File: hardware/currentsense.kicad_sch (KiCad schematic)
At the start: 12 parts, among them U801 CC6900SO-5A, U802 CC6900SO-5A, U803 CC6900SO-5A

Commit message: finish component selection
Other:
- company: (none) -> matei repair lab
- title: (none) -> HALL CURRENT SENSING
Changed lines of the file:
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@@
 (kicad_sch (version 20230121) (generator eeschema)
   (paper "A4")
+  (title_block
+    (title "HALL CURRENT SENSING")
+    (date "2023-10-11")
+    (rev "0.1")
+    (company "matei repair lab")
+  )
   (junction (at 113.03 88.9) (diameter 0) (color 0 0 0 0)
   )
@@
     (pin "1")
     (instances
-      (project "sfoc-stepper"
+      (project "lemon-pepper"
         (path "/0306e2fa-4433-4288-91d9-65a3484207ad/41d11f3b-333a-47c0-a126-1f991ee11e83"
           (reference "#PWR0803") (unit 1)
@@
     (pin "2")
     (instances
-      (project "sfoc-stepper"
+      (project "lemon-pepper"
         (path "/0306e2fa-4433-4288-91d9-65a3484207ad/41d11f3b-333a-47c0-a126-1f991ee11e83"
           (reference "R806") (unit 1)
@@
     (pin "1")
     (instances
-      (project "sfoc-stepper"
+      (project "lemon-pepper"
         (path "/0306e2fa-4433-4288-91d9-65a3484207ad/41d11f3b-333a-47c0-a126-1f991ee11e83"
           (reference "#PWR0804") (unit 1)
@@
     (pin "1")
     (instances
-      (project "sfoc-stepper"
+      (project "lemon-pepper"
         (path "/0306e2fa-4433-4288-91d9-65a3484207ad/41d11f3b-333a-47c0-a126-1f991ee11e83"
           (reference "#PWR0801") (unit 1)
@@
     (pin "8")
     (instances
-      (project "sfoc-stepper"
+      (project "lemon-pepper"
         (path "/0306e2fa-4433-4288-91d9-65a3484207ad/41d11f3b-333a-47c0-a126-1f991ee11e83"
           (reference "U802") (unit 1)
@@
     (pin "1")
     (instances
-      (project "sfoc-stepper"
+      (project "lemon-pepper"
         (path "/0306e2fa-4433-4288-91d9-65a3484207ad/41d11f3b-333a-47c0-a126-1f991ee11e83"
           (reference "#PWR0809") (unit 1)
@@
     (pin "2")
     (instances
-      (project "sfoc-stepper"
+      (project "lemon-pepper"
         (path "/0306e2fa-4433-4288-91d9-65a3484207ad/41d11f3b-333a-47c0-a126-1f991ee11e83"
           (reference "R803") (unit 1)
@@
     (pin "2")
     (instances
-      (project "sfoc-stepper"
+      (project "lemon-pepper"
         (path "/0306e2fa-4433-4288-91d9-65a3484207ad/41d11f3b-333a-47c0-a126-1f991ee11e83"
           (reference "R801") (unit 1)
@@
     (pin "2")
     (instances
-      (project "sfoc-stepper"
+      (project "lemon-pepper"
         (path "/0306e2fa-4433-4288-91d9-65a3484207ad/41d11f3b-333a-47c0-a126-1f991ee11e83"
           (reference "R805") (unit 1)
@@
     (pin "2")
     (instances
-      (project "sfoc-stepper"
+      (project "lemon-pepper"
         (path "/0306e2fa-4433-4288-91d9-65a3484207ad/41d11f3b-333a-47c0-a126-1f991ee11e83"
           (reference "R804") (unit 1)
@@
     (pin "8")
     (instances
-      (project "sfoc-stepper"
+      (project "lemon-pepper"
         (path "/0306e2fa-4433-4288-91d9-65a3484207ad/41d11f3b-333a-47c0-a126-1f991ee11e83"
           (reference "U801") (unit 1)
@@
     (pin "1")
     (instances
-      (project "sfoc-stepper"
+      (project "lemon-pepper"
         (path "/0306e2fa-4433-4288-91d9-65a3484207ad/41d11f3b-333a-47c0-a126-1f991ee11e83"
           (reference "#PWR0807") (unit 1)
@@
     (pin "8")
     (instances
-      (project "sfoc-stepper"
+      (project "lemon-pepper"
         (path "/0306e2fa-4433-4288-91d9-65a3484207ad/41d11f3b-333a-47c0-a126-1f991ee11e83"
           (reference "U803") (unit 1)
@@
     (pin "1")
     (instances
-      (project "sfoc-stepper"
+      (project "lemon-pepper"
         (path "/0306e2fa-4433-4288-91d9-65a3484207ad/41d11f3b-333a-47c0-a126-1f991ee11e83"
           (reference "#PWR0808") (unit 1)
@@
     (pin "2")
     (instances
-      (project "sfoc-stepper"
+      (project "lemon-pepper"
         (path "/0306e2fa-4433-4288-91d9-65a3484207ad/41d11f3b-333a-47c0-a126-1f991ee11e83"
           (reference "R802") (unit 1)
@@
     (pin "1")
     (instances
-      (project "sfoc-stepper"
+      (project "lemon-pepper"
         (path "/0306e2fa-4433-4288-91d9-65a3484207ad/41d11f3b-333a-47c0-a126-1f991ee11e83"
           (reference "#PWR0806") (unit 1)
@@
     (pin "1")
     (instances
-      (project "sfoc-stepper"
+      (project "lemon-pepper"
         (path "/0306e2fa-4433-4288-91d9-65a3484207ad/41d11f3b-333a-47c0-a126-1f991ee11e83"
           (reference "#PWR0805") (unit 1)
@@
     (pin "2")
     (instances
-      (project "sfoc-stepper"
+      (project "lemon-pepper"
         (path "/0306e2fa-4433-4288-91d9-65a3484207ad/41d11f3b-333a-47c0-a126-1f991ee11e83"
           (reference "C802") (unit 1)
@@
     (pin "1")
     (instances
-      (project "sfoc-stepper"
+      (project "lemon-pepper"
         (path "/0306e2fa-4433-4288-91d9-65a3484207ad/41d11f3b-333a-47c0-a126-1f991ee11e83"
           (reference "#PWR0802") (unit 1)
@@
     (pin "2")
     (instances
-      (project "sfoc-stepper"
+      (project "lemon-pepper"
         (path "/0306e2fa-4433-4288-91d9-65a3484207ad/41d11f3b-333a-47c0-a126-1f991ee11e83"
           (reference "C801") (unit 1)
@@
     (pin "2")
     (instances
-      (project "sfoc-stepper"
+      (project "lemon-pepper"
         (path "/0306e2fa-4433-4288-91d9-65a3484207ad/41d11f3b-333a-47c0-a126-1f991ee11e83"
           (reference "C803") (unit 1)

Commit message: try new driver
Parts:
- removed R801, R802, R803: 20k, Resistor_SMD:R_0402_1005Metric, symbol Device:R_Small_US
- removed R804, R805, R806: 10k, Resistor_SMD:R_0402_1005Metric, symbol Device:R_Small_US
- removed U801, U802, U803: CC6900SO-5A, easyeda2kicad:SOP-8_L4.9-W3.9-P1.27-LS6.0-BL, symbol easyeda2kicad:CC6900SO-5A
- added U701, U702, U703: ACS711KEXLT-31AB-T, easyeda2kicad:IC-SMD_ACS711KEXLT-15AB-T, symbol easyeda2kicad:ACS711KEXLT-31AB-T
- renumbered C801 to C701, C802 to C702, C803 to C703
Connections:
- net GND: now also U701.10 (NC), U701.5 (GND), U701.7 (NC), U701.8 (NC), U701.9 (NC), U702.10 (NC), U702.5 (GND), U702.7 (NC), U702.8 (NC), U702.9 (NC), U703.10 (NC), U703.5 (GND), U703.7 (NC), U703.8 (NC), U703.9 (NC)
- net U_IN: now also U701.1 (IP+)
- net U_OUT: now also U701.2 (IP-)
- net U_SENSE: now also U701.11 (VIOUT)
- net V_IN: now also U702.1 (IP+)
- net V_OUT: now also U702.2 (IP-)
- net V_SENSE: now also U702.11 (VIOUT)
- net W_IN: now also U703.1 (IP+)
- net W_OUT: now also U703.2 (IP-)
- net W_SENSE: now also U703.11 (VIOUT)
- new net +3V3: U701.12 (VCC), U702.12 (VCC), U703.12 (VCC)
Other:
- moved on the sheet: C701, C702, C703

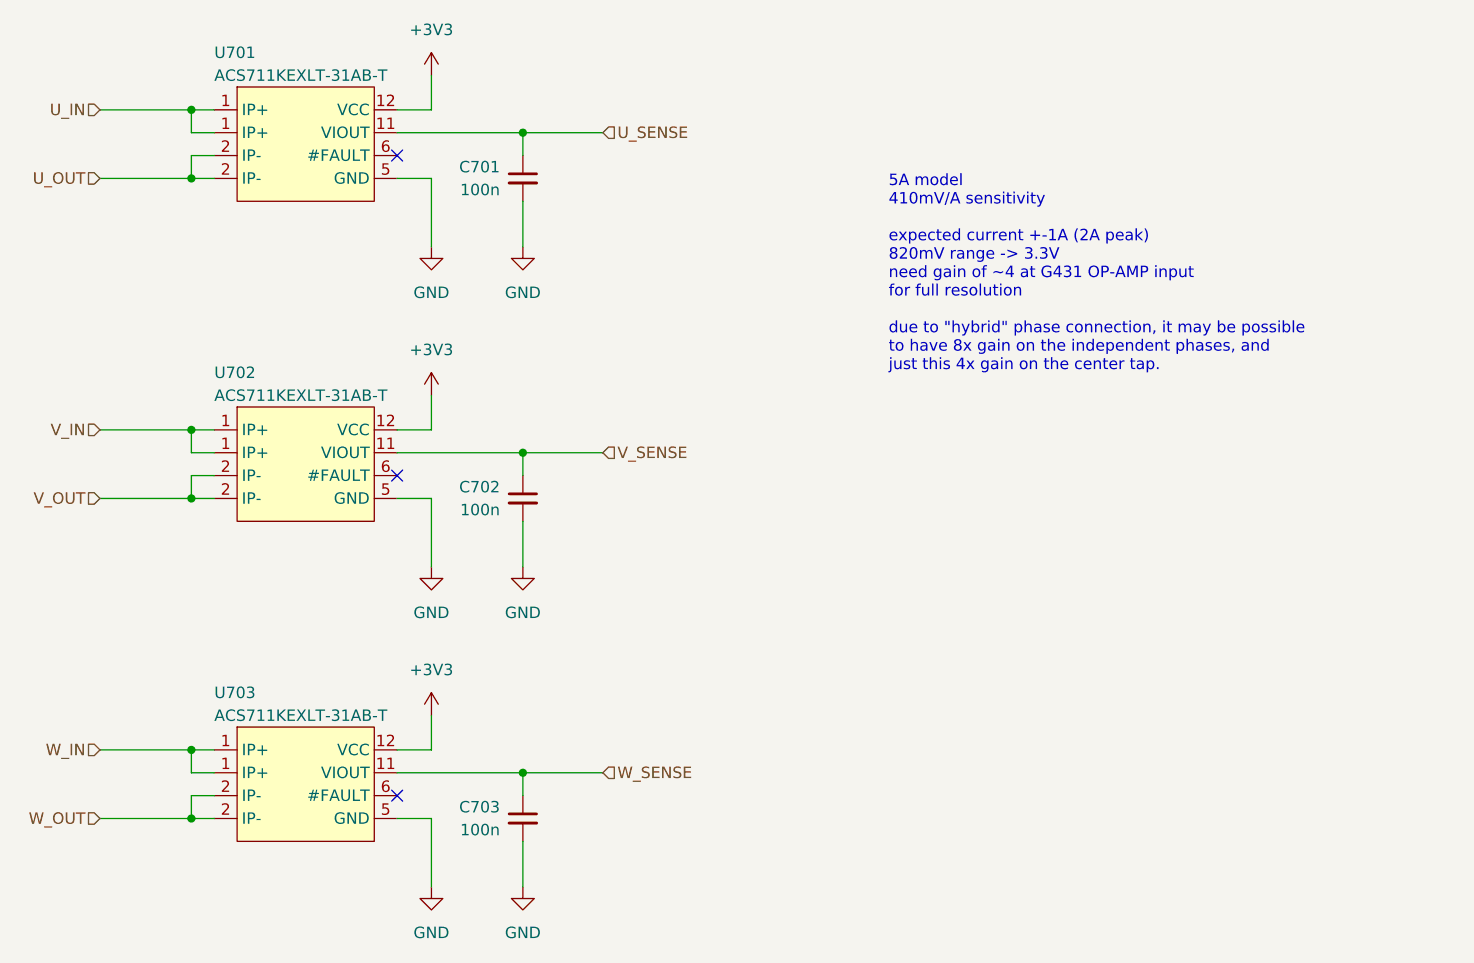
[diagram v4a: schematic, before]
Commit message: rework power plane
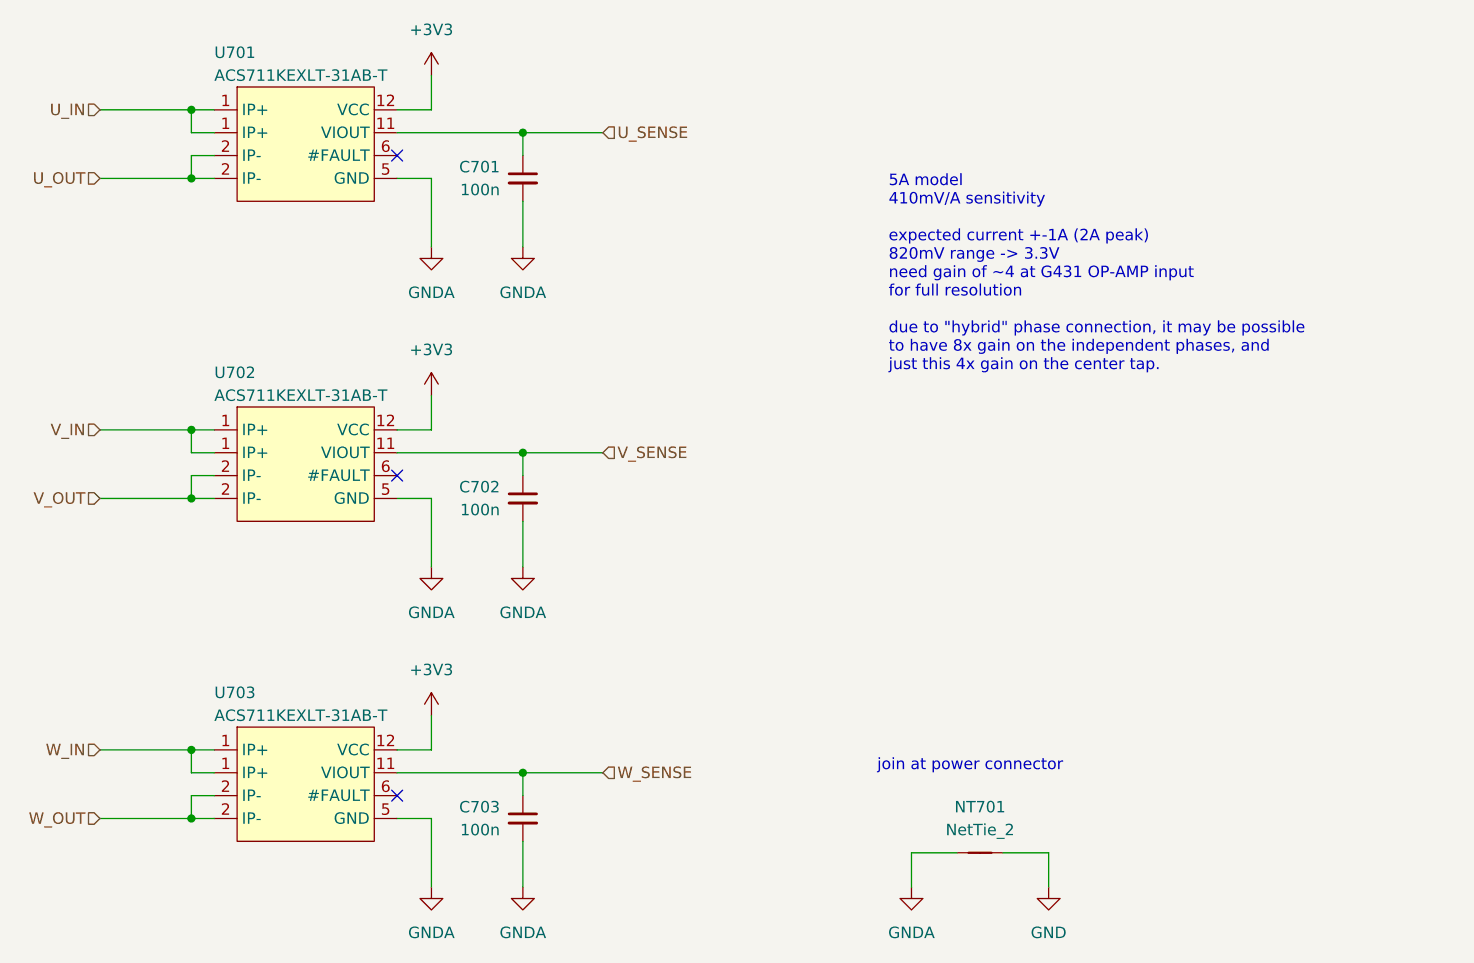
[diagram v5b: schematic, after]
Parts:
- added NT701: NetTie_2, NetTie:NetTie-2_SMD_Pad0.5mm, symbol Device:NetTie_2
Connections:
- net GND: now also NT701.2; no longer C701.2, C702.2, C703.2, U701.10 (NC), U701.5 (GND), U701.7 (NC), U701.8 (NC), U701.9 (NC), U702.10 (NC), U702.5 (GND), U702.7 (NC), U702.8 (NC), U702.9 (NC), U703.10 (NC), U703.5 (GND), U703.7 (NC), U703.8 (NC), U703.9 (NC)
- new net GNDA: C701.2, C702.2, C703.2, NT701.1, U701.10 (NC), U701.5 (GND), U701.7 (NC), U701.8 (NC), U701.9 (NC), U702.10 (NC), U702.5 (GND), U702.7 (NC), U702.8 (NC), U702.9 (NC), U703.10 (NC), U703.5 (GND), U703.7 (NC), U703.8 (NC), U703.9 (NC)
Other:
- note added: "join at power connector"
